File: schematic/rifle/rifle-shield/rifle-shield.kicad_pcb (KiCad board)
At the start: 2 copper layers, 61.3 x 34.3 mm, 59 parts, among them K1 CONN_3, K2 CONN_3, P1 USB, P10 MCU2, P12 NRF24L01, P13 IR_LED, P15 Vibro&flash, P2 MCU1, P3 Mag&fireMode, P4 VCC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

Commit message: Head and rifle boards done
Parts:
- C5: value 0.1uF -> C
- P8: footprint PIN_ARRAY_5x2 -> PIN_ARRAY_5x2_SOCKET
- R4, R5: value 10k -> R
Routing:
- net GND: track 76.0 -> 152.7 mm, vias 12 -> 22
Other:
- net class Default: trace_width 0.6 -> 0.254
- board text removed: "NRF24L01"
- board text removed: "USB"
- board text removed: "VCC"

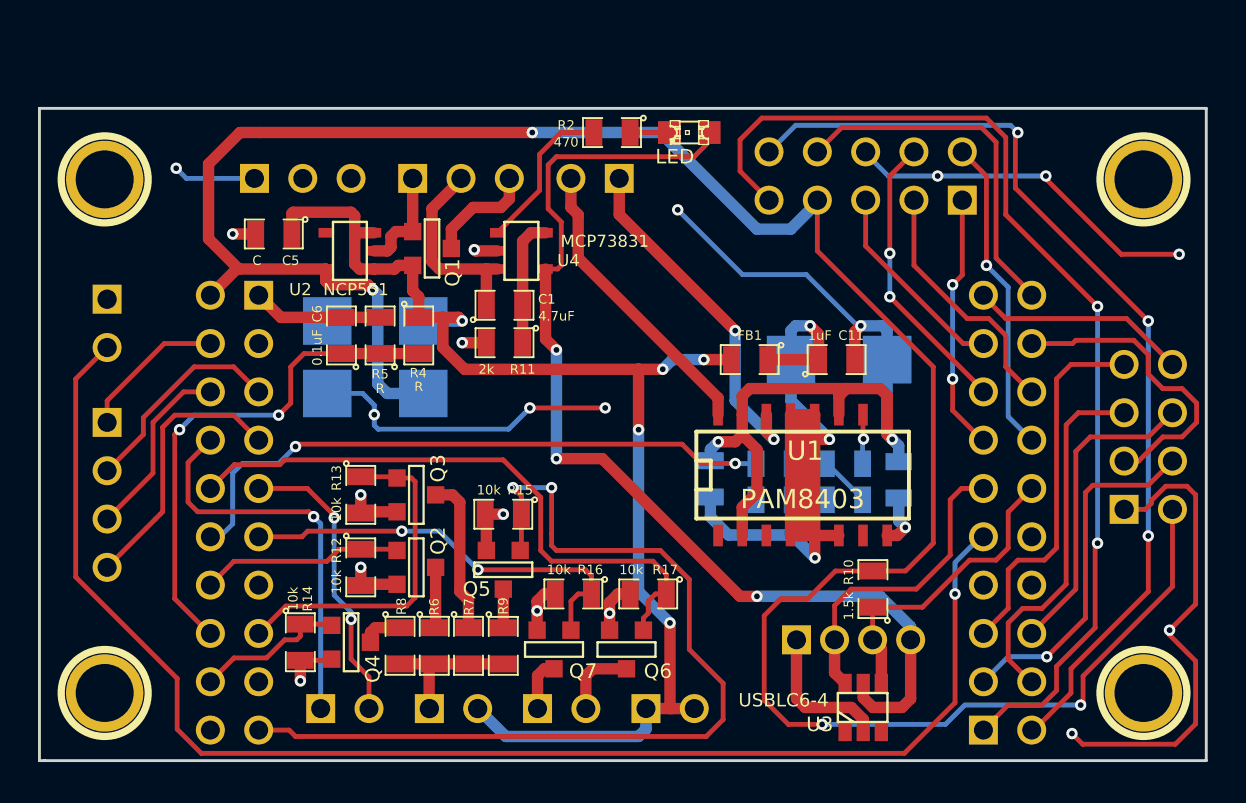
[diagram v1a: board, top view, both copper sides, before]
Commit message: Some rifle pcb improvements: led is 1206, tants are type E, hw rf swith added
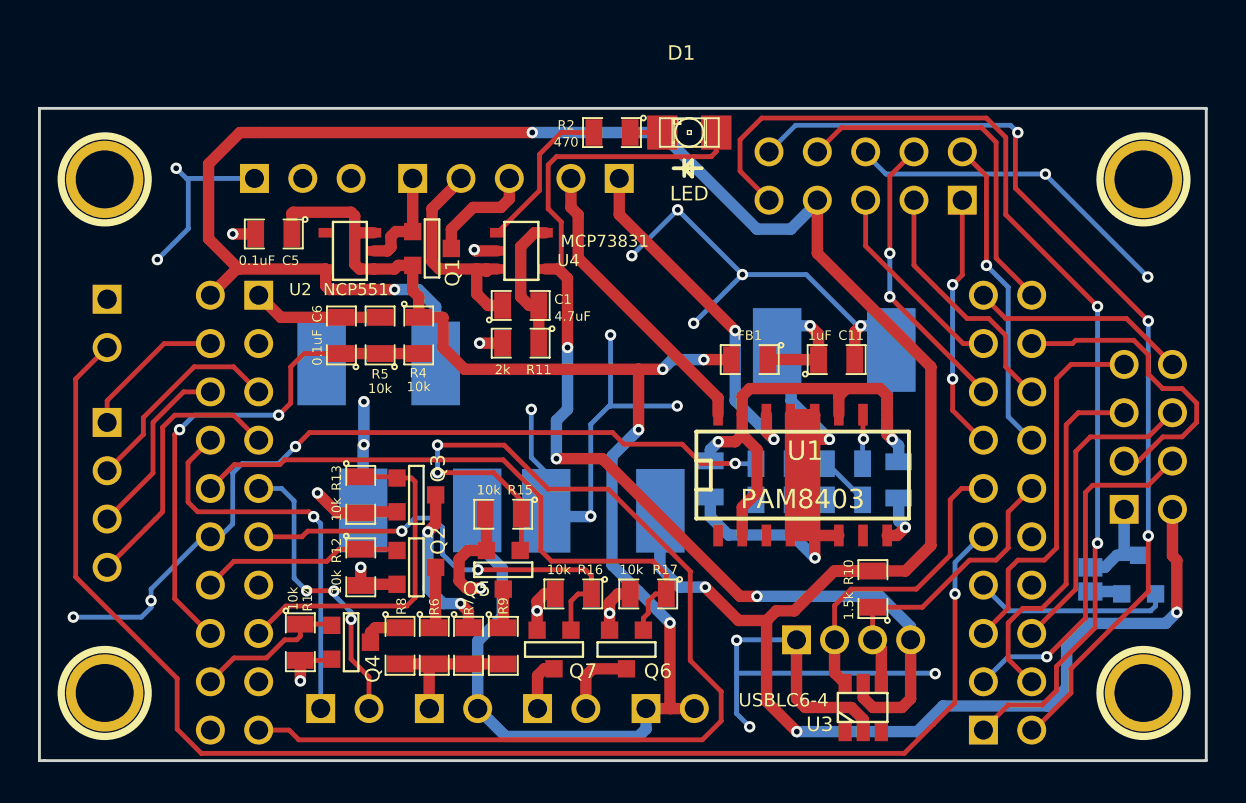
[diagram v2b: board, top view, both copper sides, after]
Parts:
- added C12: 470uF, c_tant_E, B.Cu at (73.1, 51.3)
- added JP1: nRF_ON, GS2, B.Cu at (110.5, 62.6)
- added Q8: MOSFET_N, SOT23GDS, B.Cu at (113.0, 62.4)
- C10, C7: value CP1 -> 470uF; footprint c_tant_C -> c_tant_E
- C5: value C -> 0.1uF
- C8: footprint c_tant_C -> c_tant_E
- D1: footprint LED-0805 -> LED-1206
- R4, R5: value R -> 10k
- moved C10 13.5 mm to (84.9, 59.0)
- moved C7 10.2 mm to (75.3, 59.0)
- moved R11 0.85 mm to (80.5, 50.2)
- moved C1 0.85 mm to (80.5, 48.2)
- moved C8 0.57 mm to (97.0, 50.5)
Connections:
- P10 pad 7: (no net) -> N-0000037
- P12 pad 1: GND -> N-0000036
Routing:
- net GND: track 152.7 -> 174.3 mm, vias 22 -> 29
- net +3.3V: track 124.6 -> 138.6 mm, vias 4 -> 5
- net N-0000037: track 0.00 -> 10.4 mm
- net N-000009: track 32.7 -> 42.9 mm, vias 2 -> 4
- net VCC: track 68.1 -> 77.6 mm, vias 5 -> 4
- net N-000008: track 49.6 -> 58.6 mm
- net N-0000036: track 0.00 -> 5.47 mm
- net N-0000024: track 55.8 -> 57.4 mm
- net N-0000032: track 22.3 -> 23.7 mm
- net N-0000025: track 10.8 -> 11.8 mm
- net N-0000026: track 6.72 -> 7.37 mm
- net N-000005: track 8.22 -> 8.57 mm, vias 0 -> 2
- net N-0000018: vias 2 -> 3
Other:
- net class Default: trace_width 0.254 -> 0.6
- board text added: "Caustic LT system rifle shield std rev.5"
- board text removed: "Caustic LT system rifle shield rev.4"

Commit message: New sensor module for LW round plastic sensor; leds are 1206, capacitors fixed
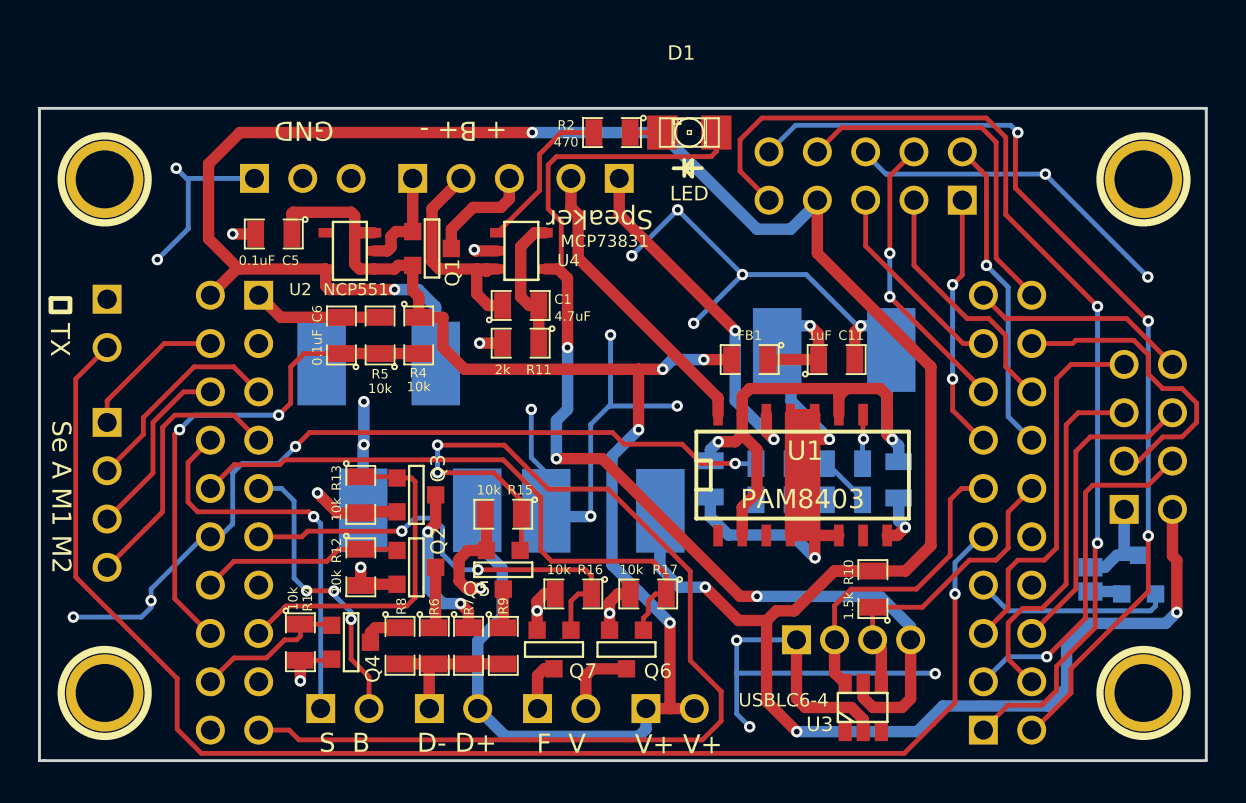
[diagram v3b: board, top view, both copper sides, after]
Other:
- board text added: "+ B+ -"
- board text added: "D- D+"
- board text added: "F V"
- board text added: "S B"
- board text added: "Se A M1 M2"
- board text added: "V+ V+"
- board text removed: "Vcc"
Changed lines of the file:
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@@
     (links 136)
     (no_connects 0)
-    (area 48.2124 35.1948 118.1576 76.747866)
+    (area 48.2124 34.31225 118.1576 76.747866)
     (thickness 1.6)
-    (drawings 28)
+    (drawings 37)
     (tracks 717)
     (zones 0)
@@
     )
   )
+  (gr_text "⏊ TX" (at 56.3118 49.3014 270) (layer F.SilkS)
+    (effects (font (size 1 1) (thickness 0.25)))
+  )
+  (gr_text "Se A M1 M2" (at 56.388 58.2803 270) (layer F.SilkS)
+    (effects (font (size 1 1) (thickness 0.25)))
+  )
+  (gr_text "S  B" (at 71.2851 71.2089) (layer F.SilkS)
+    (effects (font (size 1 1) (thickness 0.25)))
+  )
+  (gr_text "D- D+" (at 77.1906 71.2089) (layer F.SilkS)
+    (effects (font (size 1 1) (thickness 0.25)))
+  )
+  (gr_text "F  V" (at 82.677 71.247) (layer F.SilkS)
+    (effects (font (size 1 1) (thickness 0.25)))
+  )
+  (gr_text "V+ V+" (at 88.8492 71.2851) (layer F.SilkS)
+    (effects (font (size 1 1) (thickness 0.25)))
+  )
+  (gr_text GND (at 69.1515 39.0144 180) (layer F.SilkS)
+    (effects (font (size 1 1) (thickness 0.25)))
+  )
+  (gr_text "+ B+ -" (at 77.5335 39.0144 180) (layer F.SilkS)
+    (effects (font (size 1 1) (thickness 0.25)))
+  )
+  (gr_text Speaker (at 84.6963 43.6626 180) (layer F.SilkS)
+    (effects (font (size 1 1) (thickness 0.25)))
+  )
   (gr_line (start 88.5825 40.9956) (end 90.0684 40.9956) (angle 90) (layer F.SilkS) (width 0.2))
   (gr_line (start 89.1413 41.0083) (end 89.1413 40.9829) (angle 90) (layer F.SilkS) (width 0.2))
@@
   (gr_line (start 104.2289 43.9039) (end 103.3145 43.9039) (angle 90) (layer B.SilkS) (width 0.2))
   (gr_line (start 103.759 44.3738) (end 104.2289 43.9039) (angle 90) (layer B.SilkS) (width 0.2))
-  (gr_text Vcc (at 88.519 65.024) (layer B.SilkS)
+  (gr_text "V+ V+" (at 88.519 65.024) (layer B.SilkS)
     (effects (font (size 1 1) (thickness 0.25)) (justify mirror))
   )
